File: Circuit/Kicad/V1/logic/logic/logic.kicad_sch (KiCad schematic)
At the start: 4 parts

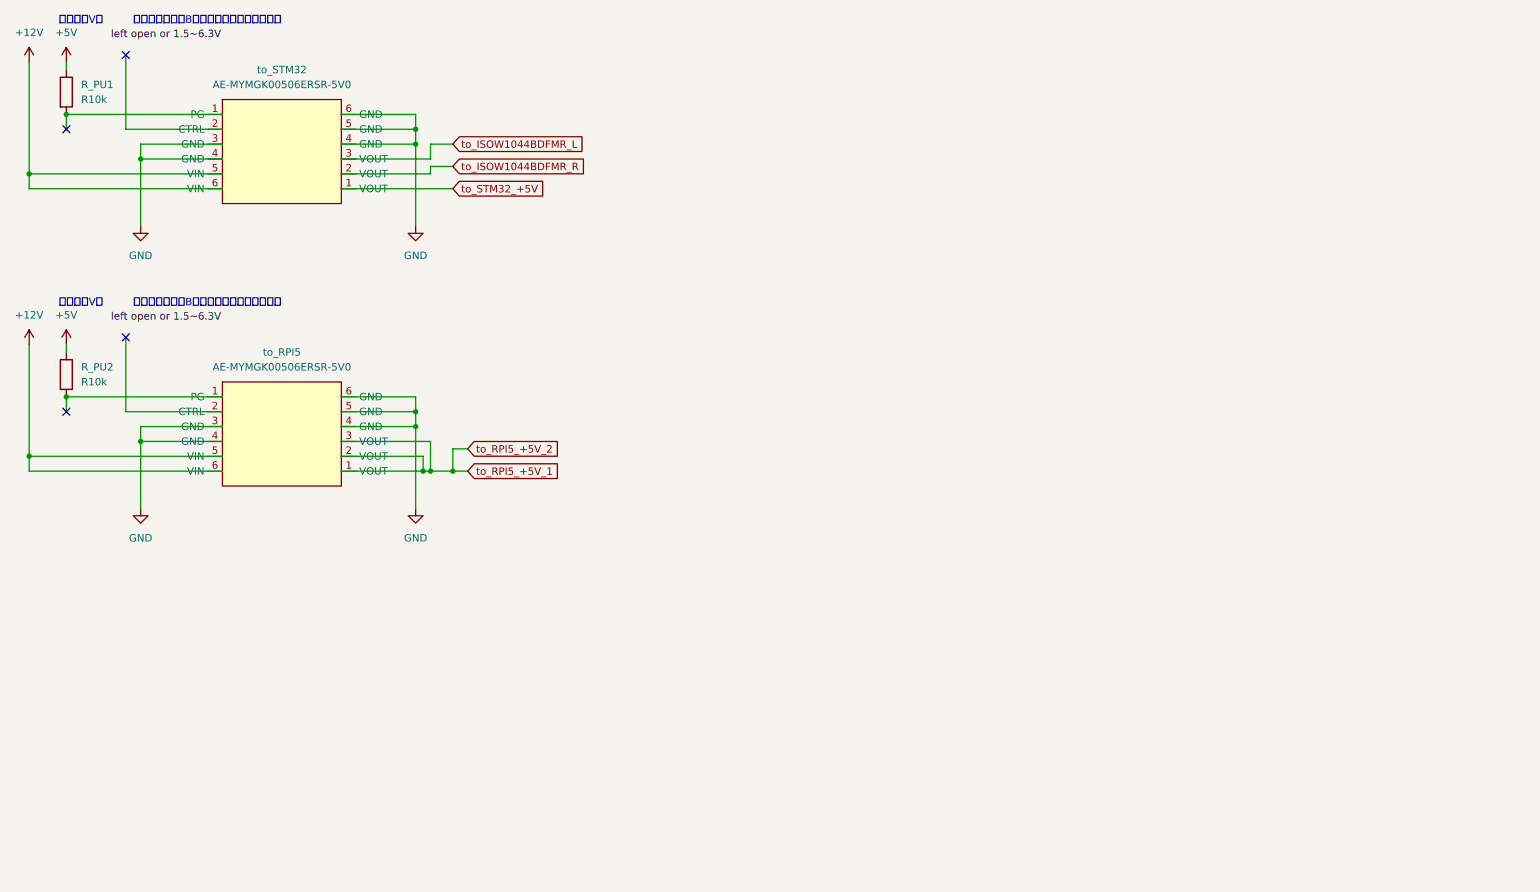
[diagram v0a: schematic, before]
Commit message: logicのsupply周りの回路のスケッチを書いた
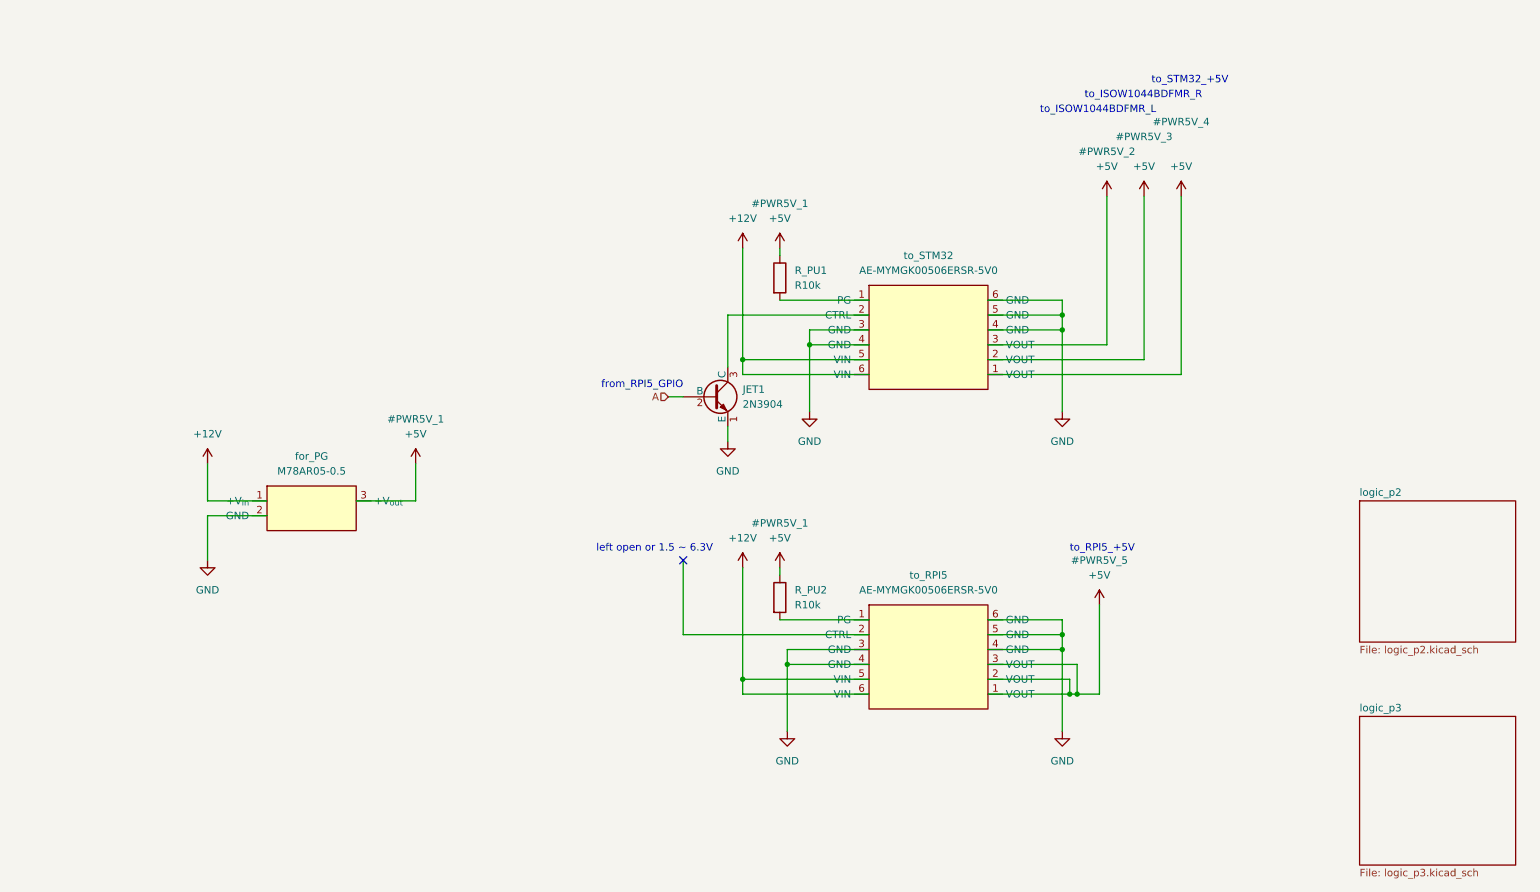
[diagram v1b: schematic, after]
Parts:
- added JET1: 2N3904, Package_TO_SOT_THT:TO-92_Inline, symbol Transistor_BJT:2N3904
- added for_PG: M78AR05-0.5, symbol DCDC_Converter:M78AR05-0.5
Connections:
- net to_ISOW1044BDFMR_L is gone; now on net GND: to_STM32.3 (VOUT)
- net to_ISOW1044BDFMR_R is gone; now on net +5V: to_STM32.2 (VOUT)
- net to_STM32_+5V is gone; now on net +5V: to_STM32.1 (VOUT)
- net +12V: now also for_PG.1 (+V_{in})
- net +5V: now also to_RPI5.1 (VOUT), to_RPI5.2 (VOUT), to_RPI5.3 (VOUT), to_STM32.3 (VOUT), for_PG.3 (+V_{out})
- net GND: now also JET1.1 (E), for_PG.2 (GND)
- removed net to_RPI5_+5V_1: to_RPI5.1 (VOUT), to_RPI5.2 (VOUT), to_RPI5.3 (VOUT)
- new net: JET1.3 (C), to_STM32.2 (VOUT)
- new net A: JET1.2 (B)
- no-connect marks 4 -> 1
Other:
- added sheet logic_p2 (logic_p2.kicad_sch)
- added sheet logic_p3 (logic_p3.kicad_sch)
- note added: "from_RPI5_GPIO"
- note added: "left open or 1.5 ~ 6.3V"
- note added: "to_ISOW1044BDFMR_L"
- note added: "to_ISOW1044BDFMR_R"
- note added: "to_RPI5_+5V"
- note added: "to_STM32_+5V"
- note removed: "どこの５V？"
- note removed: "トランジスタでB接点を作ったほうが良い？"
- moved on the sheet: R_PU1, R_PU2, to_RPI5, to_STM32

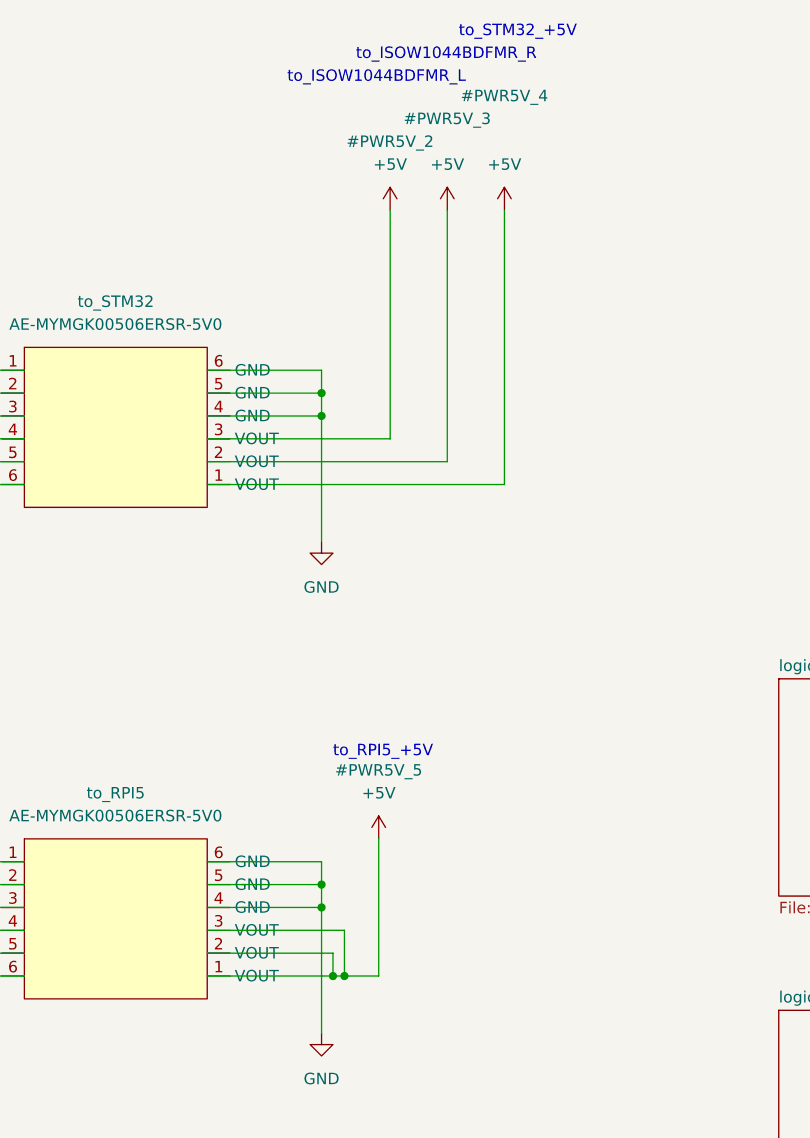
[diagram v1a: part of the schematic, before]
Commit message: version1.2.1のLogic周りの回路図を書いた
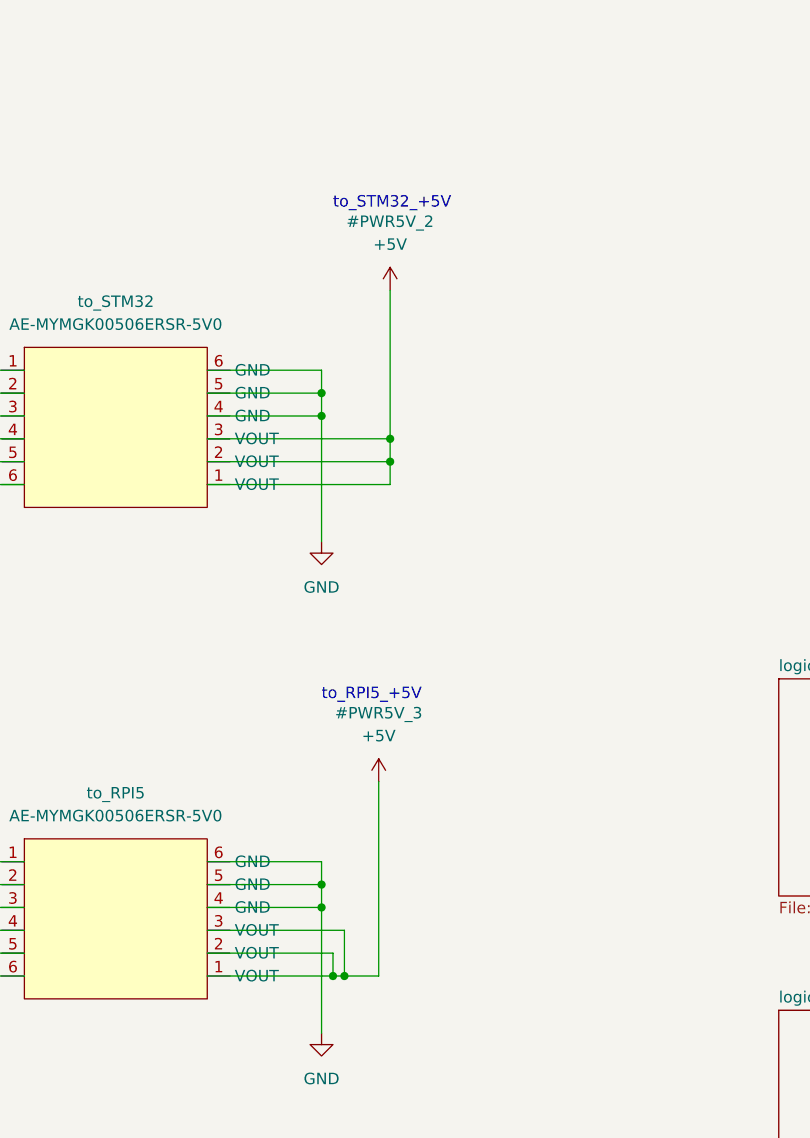
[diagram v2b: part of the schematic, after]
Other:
- note removed: "to_ISOW1044BDFMR_L"
- note removed: "to_ISOW1044BDFMR_R"
